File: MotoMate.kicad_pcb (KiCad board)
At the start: 2 copper layers, 92.3 x 50.2 mm, 65 parts, among them CN1 Cin1, CN2 Cin2, J1 Prog, J2 uUSB, J3 microSD, J4 GPS, J5 AUX_UART, J6 AUX_I2C, J7 Battery, J8 ILI9341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

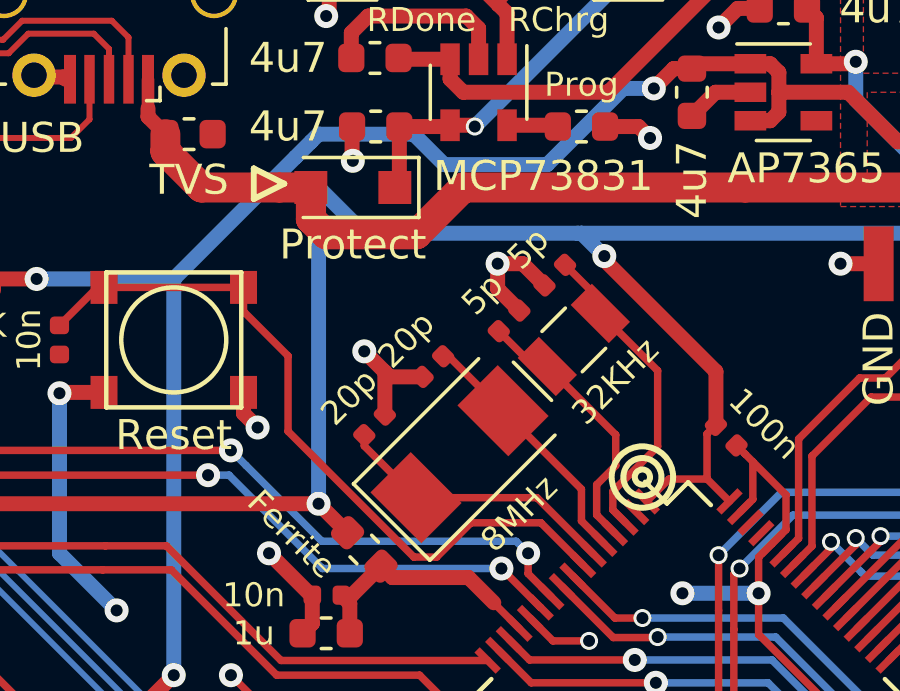
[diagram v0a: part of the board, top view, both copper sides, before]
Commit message: Round off a power trace that wound up with a weird 'elbow' shape somehow.
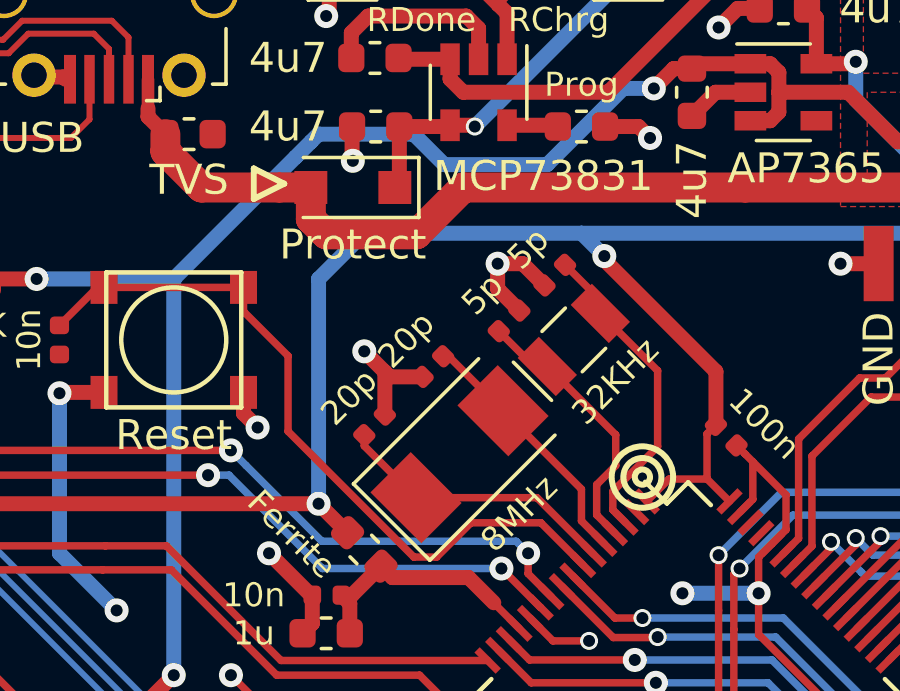
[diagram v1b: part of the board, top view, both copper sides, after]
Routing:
- net VDD: track 295.8 -> 292.7 mm
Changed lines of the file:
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@@
     (thickness 1.6)
     (drawings 35)
-    (tracks 873)
+    (tracks 872)
     (zones 0)
     (modules 65)
@@
   )
   (setup
-    (last_trace_width 0.25)
+    (last_trace_width 0.5)
     (user_trace_width 0.2)
     (user_trace_width 0.5)
@@
   (segment (start 166.835 47.31) (end 166.835 45.7785) (width 0.5) (layer F.Cu) (net 3))
   (via (at 150.241 61.976) (size 0.8) (drill 0.4) (layers F.Cu B.Cu) (net 3))
-  (segment (start 150.241 51.435) (end 150.241 61.976) (width 0.5) (layer B.Cu) (net 3))
   (segment (start 150.241 61.976) (end 151.208153 62.943153) (width 0.5) (layer F.Cu) (net 3))
   (segment (start 163.938858 61.897841) (end 163.195 61.153983) (width 0.25) (layer F.Cu) (net 3))
@@
   (segment (start 185.545 44.815) (end 185.545 53.338) (width 0.5) (layer F.Cu) (net 3))
   (segment (start 185.545 53.338) (end 185.547 53.34) (width 0.5) (layer F.Cu) (net 3))
-  (segment (start 150.241 51.435) (end 151.765 52.959) (width 0.5) (layer B.Cu) (net 3))
-  (segment (start 151.765 52.959) (end 158.877 52.959) (width 0.5) (layer B.Cu) (net 3))
   (segment (start 185.166 52.959) (end 185.547 53.34) (width 0.5) (layer B.Cu) (net 3))
   (segment (start 172.593 52.959) (end 185.166 52.959) (width 0.5) (layer B.Cu) (net 3))
@@
   (segment (start 159.766 53.848) (end 159.766 53.721) (width 0.5) (layer F.Cu) (net 3))
   (segment (start 159.766 53.721) (end 159.004 52.959) (width 0.5) (layer B.Cu) (net 3))
-  (segment (start 158.877 52.959) (end 159.004 52.959) (width 0.5) (layer B.Cu) (net 3))
   (segment (start 159.004 52.959) (end 172.593 52.959) (width 0.5) (layer B.Cu) (net 3))
   (segment (start 129.54 68.98) (end 129.54 68.18) (width 0.45) (layer F.Cu) (net 3))
@@
   (segment (start 150.15 87.793) (end 150.114 87.757) (width 0.5) (layer F.Cu) (net 3))
   (segment (start 150.15 89.367) (end 150.15 87.793) (width 0.5) (layer F.Cu) (net 3))
+  (segment (start 151.765 52.959) (end 150.241 54.483) (width 0.5) (layer B.Cu) (net 3))
+  (segment (start 159.004 52.959) (end 151.765 52.959) (width 0.5) (layer B.Cu) (net 3))
+  (segment (start 150.241 54.483) (end 150.241 61.976) (width 0.5) (layer B.Cu) (net 3))
   (segment (start 151.2825 65.3035) (end 151.003 65.024) (width 0.5) (layer F.Cu) (net 4))
   (segment (start 151.2825 66.294) (end 151.2825 65.3035) (width 0.5) (layer F.Cu) (net 4))
@@
   (segment (start 148.934 51.435) (end 149.984 51.435) (width 1) (layer F.Cu) (net 27))
   (segment (start 145.1355 49.657) (end 145.1355 50.232) (width 1) (layer F.Cu) (net 27))
-  (segment (start 160.1215 44.45) (end 158.5215 44.45) (width 0.5) (layer F.Cu) (net 80))
-  (segment (start 153.7715 44.45) (end 152.1715 44.45) (width 0.5) (layer F.Cu) (net 81))
   (segment (start 142.635883 84.787153) (end 143.804936 85.956206) (width 0.45) (layer F.Cu) (net 28))
   (segment (start 142.542847 84.787153) (end 142.635883 84.787153) (width 0.5) (layer F.Cu) (net 28))
@@
   (segment (start 131.286 70.58) (end 129.54 70.58) (width 0.25) (layer F.Cu) (net 50))
   (segment (start 131.826 71.12) (end 131.286 70.58) (width 0.25) (layer F.Cu) (net 50))
-  (segment (start 135.686 67.31) (end 135.62 67.244) (width 0.25) (layer F.Cu) (net 82))
-  (segment (start 137.49 67.31) (end 135.686 67.31) (width 0.25) (layer F.Cu) (net 82))
   (via (at 141.478 69.723) (size 0.6) (drill 0.4) (layers F.Cu B.Cu) (net 51))
   (segment (start 139.065 67.31) (end 141.478 69.723) (width 0.25) (layer F.Cu) (net 51))
@@
   (segment (start 199.644 44.45) (end 201.7775 44.45) (width 0.25) (layer B.Cu) (net 79))
   (segment (start 198.628 45.466) (end 199.644 44.45) (width 0.25) (layer B.Cu) (net 79))
+  (segment (start 160.1215 44.45) (end 158.5215 44.45) (width 0.5) (layer F.Cu) (net 80))
+  (segment (start 153.7715 44.45) (end 152.1715 44.45) (width 0.5) (layer F.Cu) (net 81))
+  (segment (start 135.686 67.31) (end 135.62 67.244) (width 0.25) (layer F.Cu) (net 82))
+  (segment (start 137.49 67.31) (end 135.686 67.31) (width 0.25) (layer F.Cu) (net 82))
   (zone (net 77) (net_name +BATT) (layer B.Cu) (hatch edge 0.508)
     (connect_pads (clearance 0.508))

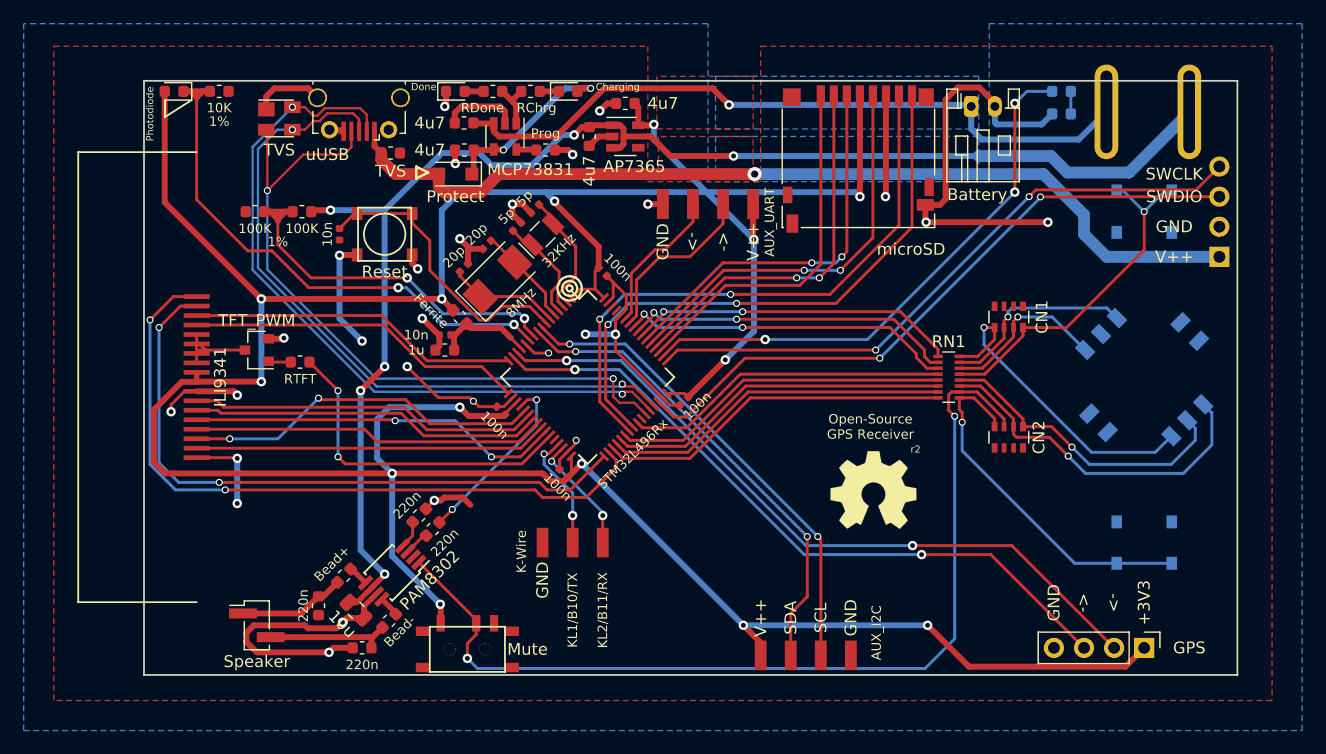
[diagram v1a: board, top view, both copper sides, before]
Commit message: Update the QFP chip footprint to have longer pads for easier soldering. Simplify the audio amp circuit. Use a smaller power switch and put it closer to the power supply. Switch voltage regulators to one which has a 'power good' pin, and connect that to the reset line.
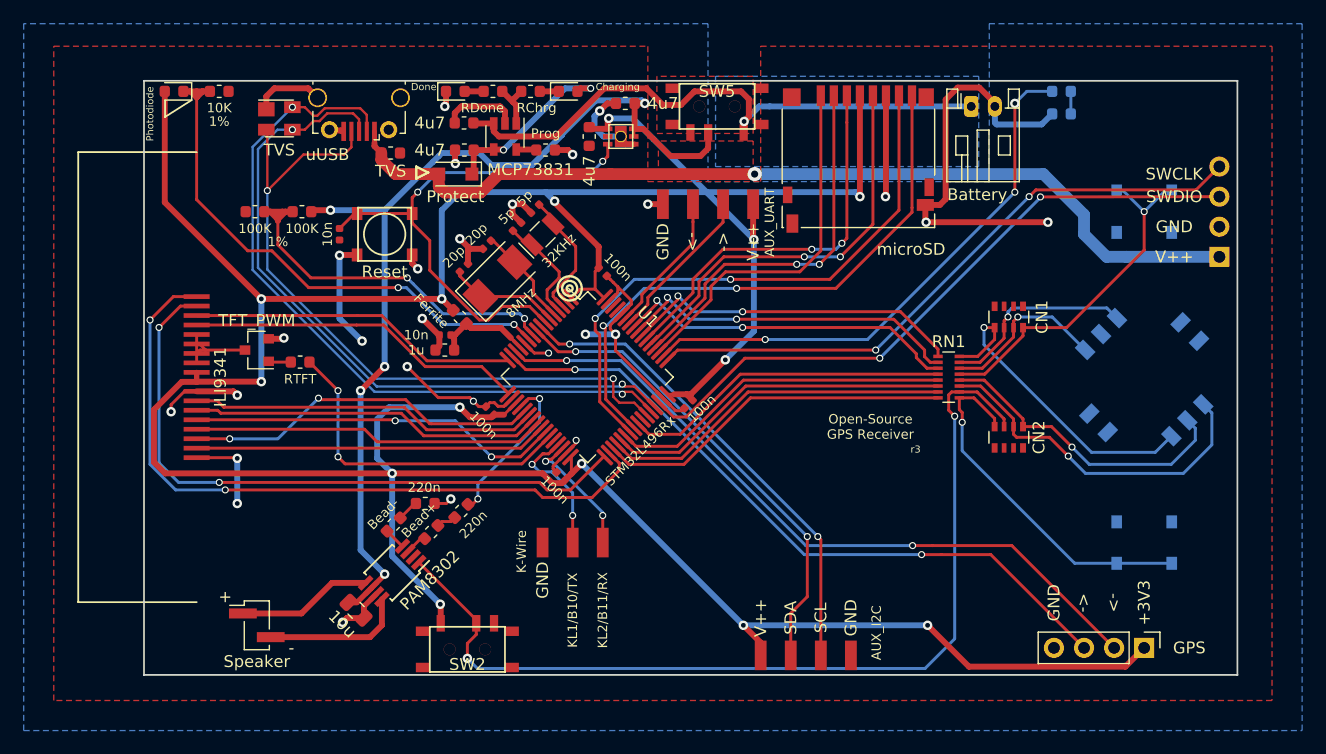
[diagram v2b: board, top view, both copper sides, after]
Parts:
- removed C14, C15: 220n, Capacitor_SMD:C_0603_1608Metric
- removed G***: LOGO, MotoMate:oshw_logo
- SW5: footprint MotoMate:SPST_Toggle_10A125V -> MotoMate:mini_slide_switch; moved to F.Cu
- U1: footprint Package_QFP:LQFP-64_10x10mm_P0.5mm -> MotoMate:LQFP-64_10x10mm_P0.5mm
- U2: value AP7365 -> LDFM33; footprint Package_TO_SOT_SMD:SOT-23-5 -> MotoMate:ST_LDFM_2x2DFN
- moved SW5 40.0 mm to (173.5, 45.7)
- moved FB2 8.24 mm to (149.4, 81.7)
- moved FB3 8.14 mm to (146.2, 81.0)
- moved C16 2.85 mm to (151.9, 79.9)
- moved C17 1.14 mm to (148.8, 79.2), turned to 0 degrees
- moved C5 0.93 mm to (154.3, 71.4)
- moved C4 0.46 mm to (171.1, 70.9)
- moved U2 0.38 mm to (165.4, 48.3)
- moved C6 0.36 mm to (160.3, 77.0)
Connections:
- C1 pad 1: VPP -> VDD
- C2 pad 2: VDD -> VPP
- FB2 pad 1: Net-(C14-Pad2) -> Net-(FB2-Pad1)
- FB2 pad 2: Net-(FB2-Pad2) -> Net-(C16-Pad1)
- FB3 pad 1: Net-(FB3-Pad1) -> Net-(C17-Pad1)
- FB3 pad 2: Net-(C15-Pad2) -> Net-(FB3-Pad2)
- LS1 pad 1: Net-(C14-Pad2) -> Net-(LS1-Pad1)
- LS1 pad 2: Net-(C15-Pad2) -> Net-(LS1-Pad2)
- SW5 pad 1: VPP -> +BATT
- SW5 pad 2: +BATT -> VPP
- U2 pad 1: VPP -> VDD
- U2 pad 2: GND -> Net-(U2-Pad2)
- U2 pad 3: VPP -> Reset
- U2 pad 4: Net-(U2-Pad4) -> GND
- U2 pad 5: VDD -> VPP
- U3 pad 3: Net-(C16-Pad1) -> Net-(FB2-Pad1)
- U3 pad 4: Net-(C17-Pad1) -> Net-(FB3-Pad2)
- U3 pad 5: Net-(FB2-Pad2) -> Net-(LS1-Pad1)
- U3 pad 8: Net-(FB3-Pad1) -> Net-(LS1-Pad2)
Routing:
- net VPP: track 120.5 -> 82.1 mm, vias 6 -> 5
- net Reset: track 24.7 -> 45.0 mm, vias 0 -> 2
- net GND: track 165.8 -> 151.7 mm, vias 28 -> 27
- net Net-(LS1-Pad2): track 0.00 -> 12.0 mm
- net Net-(LS1-Pad1): track 0.00 -> 11.4 mm
- net Net-(C15-Pad2): track 10.7 -> 0.00 mm
- net +BATT: track 59.9 -> 50.0 mm
- net Net-(C14-Pad2): track 9.08 -> 0.00 mm
- net VDD: track 292.7 -> 295.4 mm
- net Net-(FB2-Pad1): track 0.00 -> 1.87 mm
- net Net-(FB3-Pad2): track 0.00 -> 1.82 mm
- net Net-(FB3-Pad1): track 1.75 -> 0.00 mm
- net Net-(FB2-Pad2): track 1.75 -> 0.00 mm
- net Speaker: track 15.1 -> 13.6 mm
- net K-Line1: track 10.1 -> 11.6 mm
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- removed copper zone on B.Cu, net VPP
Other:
- board text added: "+"
- board text added: "-"
- board text added: "r3"
- board text removed: "r2"
